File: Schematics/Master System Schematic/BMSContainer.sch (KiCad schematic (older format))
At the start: 2 parts, among them U1 OrionBMS2, U2 OrionThermExp

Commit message: Fixed Master
Readded all the things lost in the merge on master.
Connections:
- net C_GND: no longer names the net of U1.C27 (C_Sens_GND)
- net C_High: no longer names the net of U1.C13 (C_High)
- net C_Low: no longer names the net of U1.C14 (C_Low)
- net C_Pow: no longer names the net of U1.C28 (C_Sens)
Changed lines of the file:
@@
 $Descr A 11000 8500
 encoding utf-8
-Sheet 9 13
+Sheet 4 13
 Title ""
-Date ""
+Date "2020-10-12"
 Rev ""
 Comp ""
@@
 NoConn ~ 5200 4550
 Text HLabel 2350 2650 0    50   BiDi ~ 0
-CAN+
+CAN_H
 Text HLabel 2350 2750 0    50   BiDi ~ 0
-CAN-
+CAN_L
 Entry Wire Line
 	3650 2650 3750 2750
@@
 Entry Wire Line
 	3350 6350 3450 6450
-Wire Wire Line
-	5200 1750 5300 1750
-Wire Wire Line
-	5200 1850 5300 1850
-Wire Wire Line
-	5200 2650 5300 2650
-Wire Wire Line
-	5200 2750 5300 2750
-Text HLabel 5300 2650 2    50   Input ~ 0
-C_GND
-Text HLabel 5300 2750 2    50   Input ~ 0
-C_Pow
-Text HLabel 5300 1750 2    50   Input ~ 0
-C_High
-Text HLabel 5300 1850 2    50   Input ~ 0
-C_Low
 Text HLabel 3700 3550 0    50   Output ~ 0
 BMS_Fault
@@
 Wire Bus Line
 	5600 3550 5600 3350
+Wire Wire Line
+	5200 2750 5250 2750
+Wire Wire Line
+	5200 2650 5250 2650
+Wire Wire Line
+	5200 1850 5250 1850
+Wire Wire Line
+	5200 1750 5250 1750
+Entry Wire Line
+	5250 1750 5350 1650
+Entry Wire Line
+	5250 1850 5350 1750
+Entry Wire Line
+	5250 2650 5350 2550
+Entry Wire Line
+	5250 2750 5350 2650
+Wire Bus Line
+	5350 2650 5350 2550
+Wire Bus Line
+	5350 1650 5350 1750
+Entry Bus Bus
+	5350 1650 5450 1550
+Entry Bus Bus
+	5350 2550 5450 2450
+Wire Bus Line
+	5450 1550 5600 1550
+Wire Bus Line
+	5600 1550 5600 2450
+Wire Bus Line
+	5450 2450 5600 2450
+Wire Bus Line
+	5600 1550 5900 1550
 Wire Bus Line
 	2150 5150 2150 6450
@@
 Wire Bus Line
 	6800 1450 6800 6450
+Connection ~ 5600 1550
+Text HLabel 5900 1550 2    50   Input ~ 0
+Current_Sensor
 $EndSCHEMATC

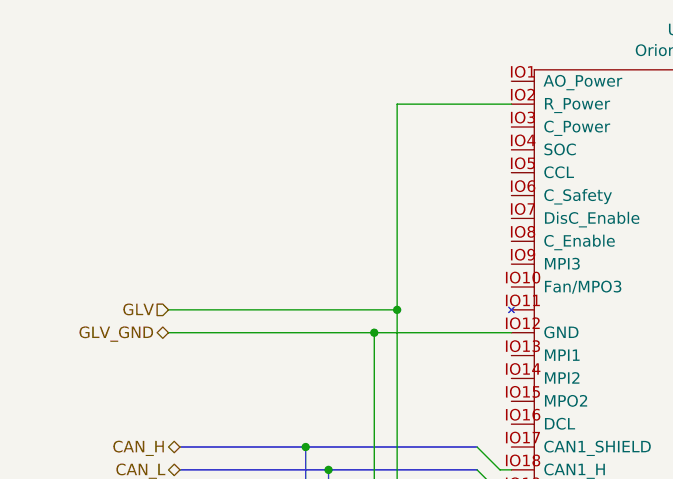
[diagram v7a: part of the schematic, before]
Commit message: Wire Runs and cleanup
>Cleaned up some wire runs
>Added Charger safety connection
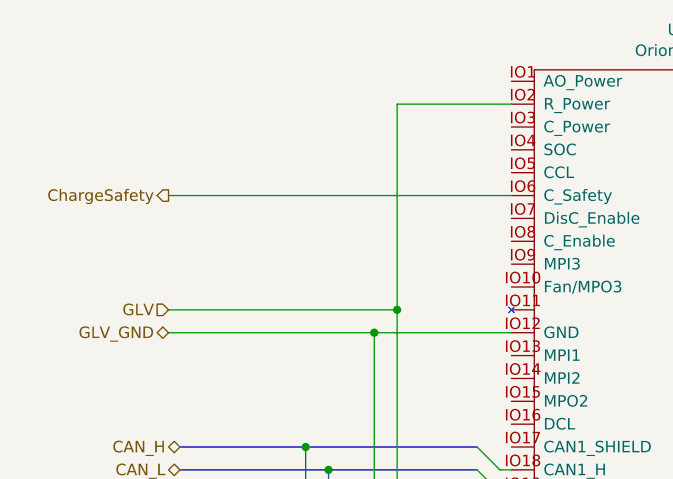
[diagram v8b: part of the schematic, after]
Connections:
- net ChargeSafety: now reaches U1.IO6 (C_Safety)
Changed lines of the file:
@@
 Wire Bus Line
 	5600 1550 5900 1550
+Connection ~ 5600 1550
+Text HLabel 5900 1550 2    50   Input ~ 0
+Current_Sensor
+Wire Wire Line
+	3800 1550 2300 1550
 Wire Bus Line
 	2150 5150 2150 6450
@@
 Wire Bus Line
 	6800 1450 6800 6450
-Connection ~ 5600 1550
-Text HLabel 5900 1550 2    50   Input ~ 0
-Current_Sensor
+Text HLabel 2300 1550 0    50   Output ~ 0
+ChargeSafety
 $EndSCHEMATC
